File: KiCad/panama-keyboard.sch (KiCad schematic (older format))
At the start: 168 parts, among them J1 AVR-ISP-6, J2 USB_C_Receptacle_USB2.0, U1 ATmega32A-PU, Y1 Crystal

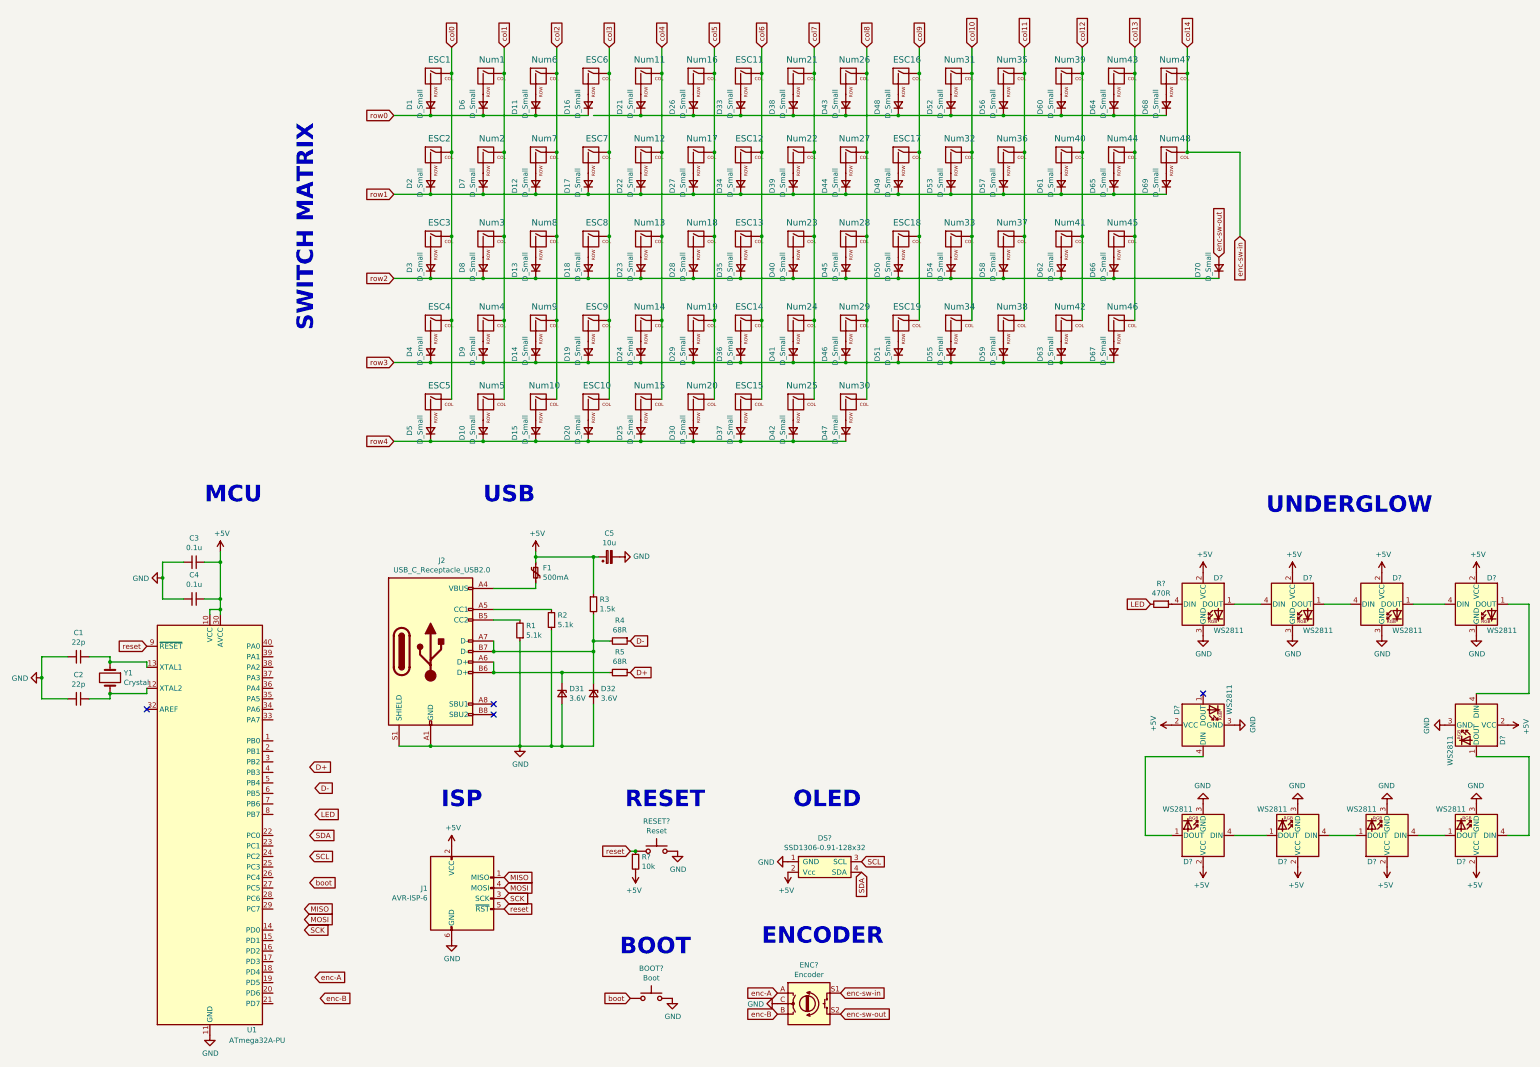
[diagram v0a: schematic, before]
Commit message: footprint added except MX
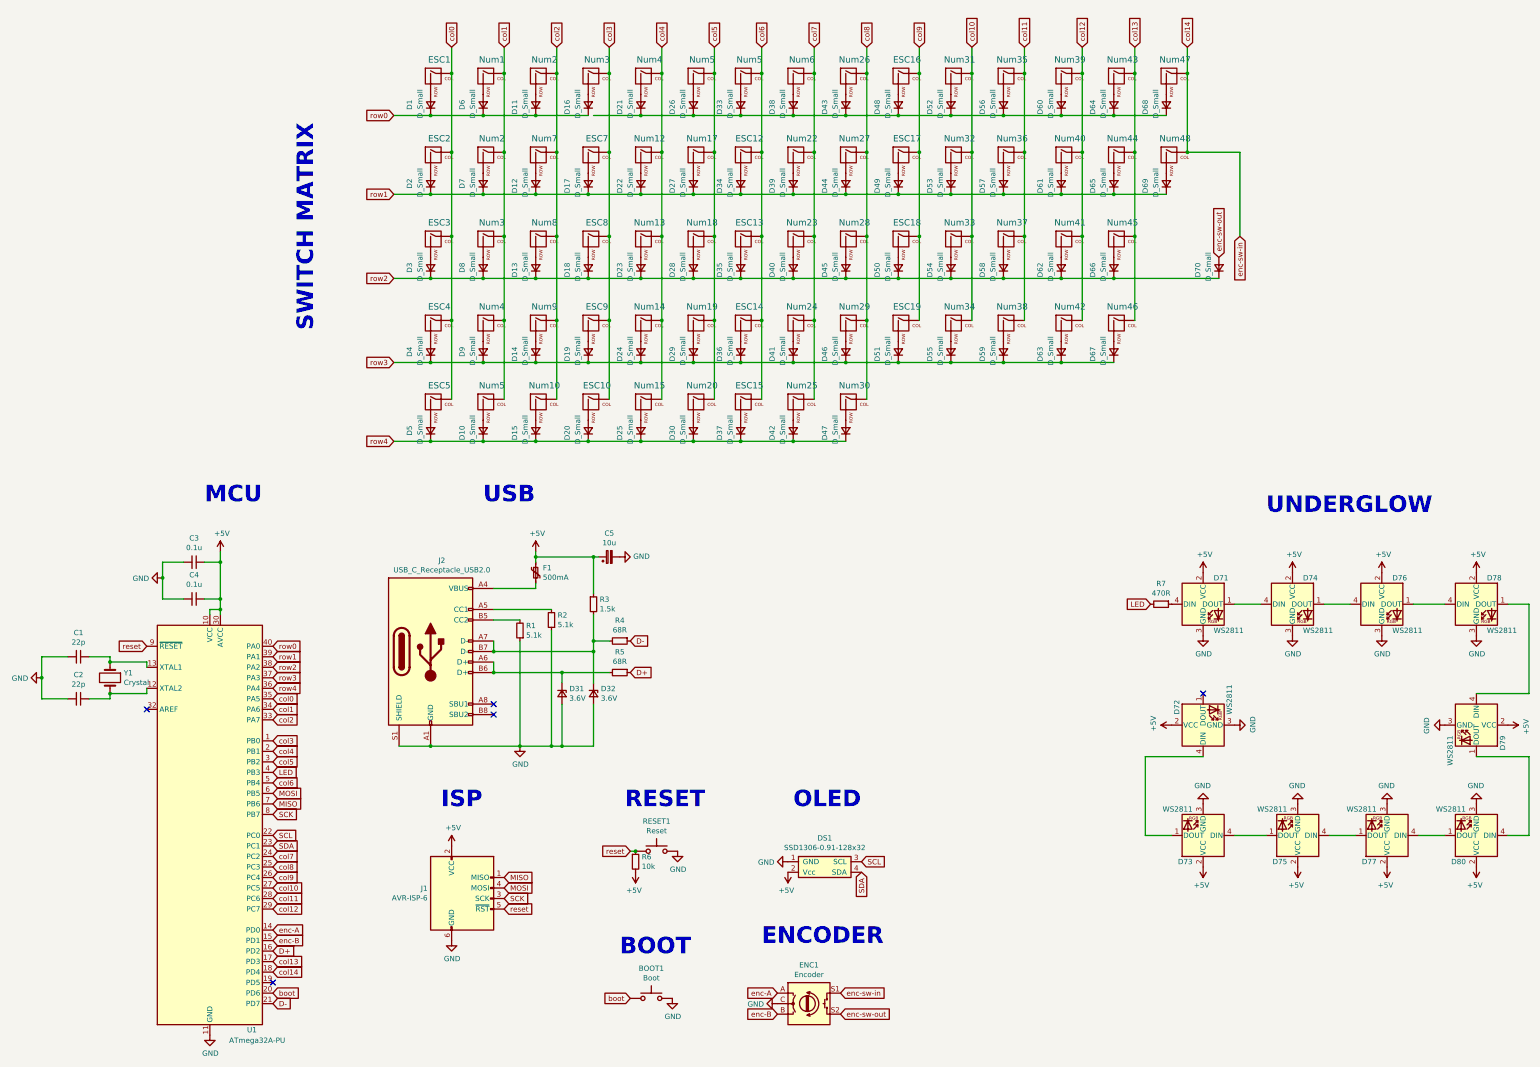
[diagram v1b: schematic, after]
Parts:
- BOOT1: renamed from BOOT?; footprint (none) -> Button_Switch_THT:SW_PUSH_6mm
- C1, C2, C3, C4: footprint (none) -> Capacitor_THT:C_Disc_D5.0mm_W2.5mm_P5.00mm
- C5: footprint (none) -> Capacitor_THT:CP_Radial_D5.0mm_P2.00mm
- D1, D10, D11, D12, D13, D14, D15, D16, D17, D18, D19, D2, D20, D21, D22, D23, D24, D25, D26, D27, D28, D29, D3, D30, D31, D32, D33, D34, D35, D36, D37, D38, D39, D4, D40, D41, D42, D43, D44, D45, D46, D47, D48, D49, D5, D50, D51, D52, D53, D54, D55, D56, D57, D58, D59, D6, D60, D61, D62, D63, D64, D65, D66, D67, D68, D69, D7, D70, D8, D9: footprint (none) -> Diode_THT:D_DO-35_SOD27_P7.62mm_Horizontal
- D71, D72, D73, D74, D75, D76, D77, D78, D79, D80: renamed from D?; footprint (none) -> LED_THT:LED_D5.0mm-4_RGB
- DS1: renamed from DS?; footprint (none) -> OLED:PinHeader_1x04_P2.54mm_Vertical
- ENC1: renamed from ENC?; footprint (none) -> Rotary_Encoder:RotaryEncoder_Alps_EC11E-Switch_Vertical_H20mm
- F1: footprint (none) -> Fuse:Fuse_BelFuse_0ZRE0005FF_L8.3mm_W3.8mm
- J1: footprint (none) -> Connector_PinHeader_2.54mm:PinHeader_2x03_P2.54mm_Vertical
- J2: footprint (none) -> Connector_USB:USB_C_Receptacle_GCT_USB4085
- R1, R2, R3, R4, R5: footprint (none) -> Resistor_THT:R_Axial_DIN0204_L3.6mm_D1.6mm_P5.08mm_Horizontal
- R6, R7: renamed from R?; footprint (none) -> Resistor_THT:R_Axial_DIN0204_L3.6mm_D1.6mm_P5.08mm_Horizontal
- RESET1: renamed from RESET?; footprint (none) -> Button_Switch_THT:SW_PUSH_6mm
- Y1: footprint (none) -> Crystal:Crystal_HC49-U_Vertical
- renumbered Num6 to Num2, ESC6 to Num3, Num11 to Num4, Num16 to Num5, ESC11 to Num5, Num21 to Num6
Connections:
- net D+: now also U1.16 (PD2)
- net D-: now also U1.21 (PD7)
- net LED: now also U1.4 (PB3)
- net MISO: now also U1.7 (PB6)
- net MOSI: now also U1.6 (PB5)
- net SCK: now also U1.8 (PB7)
- net SCL: now also U1.22 (PC0)
- net SDA: now also U1.23 (PC1)
- net boot: now also U1.20 (PD6)
- net col0: now also U1.35 (PA5)
- net col1: now also U1.34 (PA6)
- net col10: now also U1.27 (PC5)
- net col11: now also U1.28 (PC6)
- net col12: now also U1.29 (PC7)
- net col13: now also U1.17 (PD3)
- net col14: now also U1.18 (PD4)
- net col2: now also U1.33 (PA7)
- net col3: now also U1.1 (PB0)
- net col4: now also U1.2 (PB1)
- net col5: now also U1.3 (PB2)
- net col6: now also U1.5 (PB4)
- net col7: now also U1.24 (PC2)
- net col8: now also U1.25 (PC3)
- net col9: now also U1.26 (PC4)
- net enc-A: now also U1.14 (PD0)
- net enc-B: now also U1.15 (PD1)
- net row0: now also U1.40 (PA0)
- net row1: now also U1.39 (PA1)
- net row2: now also U1.38 (PA2)
- net row3: now also U1.37 (PA3)
- net row4: now also U1.36 (PA4)
- no-connect marks 4 -> 5

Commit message: finished w1 schematic, started PCB
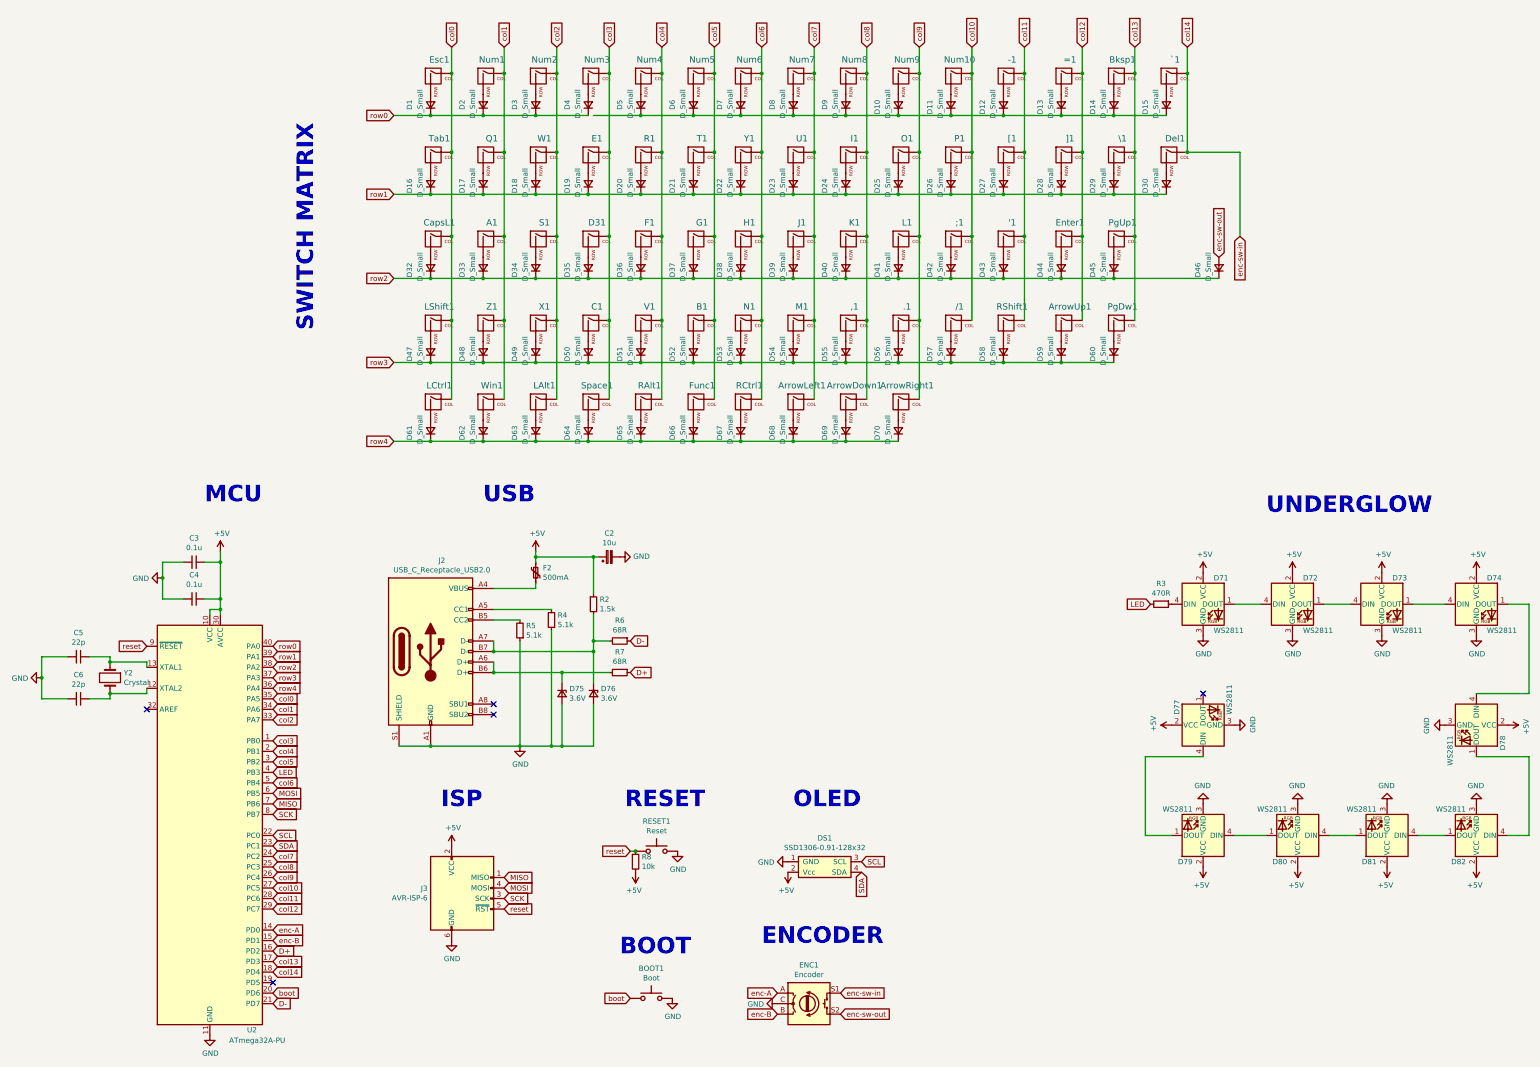
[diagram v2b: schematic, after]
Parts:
- added D67: D_Small, Diode_THT:D_DO-35_SOD27_P7.62mm_Horizontal, symbol Device:D_Small
- added RCtrl1: MX, Button_Switch_Keyboard:SW_Cherry_MX_1.00u_PCB, symbol Keyboard:MX
- '1: renamed from Num37; footprint (none) -> Button_Switch_Keyboard:SW_Cherry_MX_1.00u_PCB
- ,1: renamed from Num29; footprint (none) -> Button_Switch_Keyboard:SW_Cherry_MX_1.00u_PCB
- -1: renamed from Num35; footprint (none) -> Button_Switch_Keyboard:SW_Cherry_MX_1.00u_PCB
- .1: renamed from ESC19; footprint (none) -> Button_Switch_Keyboard:SW_Cherry_MX_1.00u_PCB
- /1: renamed from Num34; footprint (none) -> Button_Switch_Keyboard:SW_Cherry_MX_1.00u_PCB
- ;1: renamed from Num33; footprint (none) -> Button_Switch_Keyboard:SW_Cherry_MX_1.00u_PCB
- =1: renamed from Num39; footprint (none) -> Button_Switch_Keyboard:SW_Cherry_MX_1.00u_PCB
- A1: renamed from Num3; footprint (none) -> Button_Switch_Keyboard:SW_Cherry_MX_1.00u_PCB
- ArrowDown1: renamed from Num25; footprint (none) -> Button_Switch_Keyboard:SW_Cherry_MX_1.00u_PCB
- ArrowLeft1: renamed from ESC15; footprint (none) -> Button_Switch_Keyboard:SW_Cherry_MX_1.00u_PCB
- ArrowRight1: renamed from Num30; footprint (none) -> Button_Switch_Keyboard:SW_Cherry_MX_1.00u_PCB
- ArrowUp1: renamed from Num42; footprint (none) -> Button_Switch_Keyboard:SW_Cherry_MX_1.00u_PCB
- B1: renamed from Num19; footprint (none) -> Button_Switch_Keyboard:SW_Cherry_MX_1.00u_PCB
- Bksp1: renamed from Num43; footprint (none) -> Button_Switch_Keyboard:SW_Cherry_MX_2.00u_PCB
- C1: renamed from ESC9; footprint (none) -> Button_Switch_Keyboard:SW_Cherry_MX_1.00u_PCB
- CapsL1: renamed from ESC3; footprint (none) -> Button_Switch_Keyboard:SW_Cherry_MX_1.75u_PCB
- D31: renamed from ESC8; footprint (none) -> Button_Switch_Keyboard:SW_Cherry_MX_1.00u_PCB
- Del1: renamed from Num48; footprint (none) -> Button_Switch_Keyboard:SW_Cherry_MX_1.00u_PCB
- E1: renamed from ESC7; footprint (none) -> Button_Switch_Keyboard:SW_Cherry_MX_1.00u_PCB
- Enter1: renamed from Num41; footprint (none) -> Button_Switch_Keyboard:SW_Cherry_MX_2.25u_PCB
- Esc1: renamed from ESC1; footprint (none) -> Button_Switch_Keyboard:SW_Cherry_MX_1.00u_PCB
- F1: renamed from Num13; footprint (none) -> Button_Switch_Keyboard:SW_Cherry_MX_1.00u_PCB
- Func1: renamed from Num20; footprint (none) -> Button_Switch_Keyboard:SW_Cherry_MX_1.00u_PCB
- G1: renamed from Num18; footprint (none) -> Button_Switch_Keyboard:SW_Cherry_MX_1.00u_PCB
- H1: renamed from ESC13; footprint (none) -> Button_Switch_Keyboard:SW_Cherry_MX_1.00u_PCB
- I1: renamed from Num27; footprint (none) -> Button_Switch_Keyboard:SW_Cherry_MX_1.00u_PCB
- J1: renamed from Num23; footprint (none) -> Button_Switch_Keyboard:SW_Cherry_MX_1.00u_PCB
- K1: renamed from Num28; footprint (none) -> Button_Switch_Keyboard:SW_Cherry_MX_1.00u_PCB
- L1: renamed from ESC18; footprint (none) -> Button_Switch_Keyboard:SW_Cherry_MX_1.00u_PCB
- LAlt1: renamed from Num10; footprint (none) -> Button_Switch_Keyboard:SW_Cherry_MX_1.25u_PCB
- LCtrl1: renamed from ESC5; footprint (none) -> Button_Switch_Keyboard:SW_Cherry_MX_1.25u_PCB
- LShift1: renamed from ESC4; footprint (none) -> Button_Switch_Keyboard:SW_Cherry_MX_2.25u_PCB
- M1: renamed from Num24; footprint (none) -> Button_Switch_Keyboard:SW_Cherry_MX_1.00u_PCB
- N1: renamed from ESC14; footprint (none) -> Button_Switch_Keyboard:SW_Cherry_MX_1.00u_PCB
- Num1, Num2, Num3, Num4, Num5: footprint (none) -> Button_Switch_Keyboard:SW_Cherry_MX_1.00u_PCB
- Num10: renamed from Num31; footprint (none) -> Button_Switch_Keyboard:SW_Cherry_MX_1.00u_PCB
- Num6: renamed from Num5; footprint (none) -> Button_Switch_Keyboard:SW_Cherry_MX_1.00u_PCB
- Num7: renamed from Num6; footprint (none) -> Button_Switch_Keyboard:SW_Cherry_MX_1.00u_PCB
- Num8: renamed from Num26; footprint (none) -> Button_Switch_Keyboard:SW_Cherry_MX_1.00u_PCB
- Num9: renamed from ESC16; footprint (none) -> Button_Switch_Keyboard:SW_Cherry_MX_1.00u_PCB
- O1: renamed from ESC17; footprint (none) -> Button_Switch_Keyboard:SW_Cherry_MX_1.00u_PCB
- P1: renamed from Num32; footprint (none) -> Button_Switch_Keyboard:SW_Cherry_MX_1.00u_PCB
- PgDw1: renamed from Num46; footprint (none) -> Button_Switch_Keyboard:SW_Cherry_MX_1.00u_PCB
- PgUp1: renamed from Num45; footprint (none) -> Button_Switch_Keyboard:SW_Cherry_MX_1.00u_PCB
- Q1: renamed from Num2; footprint (none) -> Button_Switch_Keyboard:SW_Cherry_MX_1.00u_PCB
- R1: renamed from Num12; footprint (none) -> Button_Switch_Keyboard:SW_Cherry_MX_1.00u_PCB
- RAlt1: renamed from Num15; footprint (none) -> Button_Switch_Keyboard:SW_Cherry_MX_1.00u_PCB
- RShift1: renamed from Num38; footprint (none) -> Button_Switch_Keyboard:SW_Cherry_MX_1.75u_PCB
- S1: renamed from Num8; footprint (none) -> Button_Switch_Keyboard:SW_Cherry_MX_1.00u_PCB
- Space1: renamed from ESC10; footprint (none) -> Button_Switch_Keyboard:SW_Cherry_MX_6.25u_PCB
- T1: renamed from Num17; footprint (none) -> Button_Switch_Keyboard:SW_Cherry_MX_1.00u_PCB
- Tab1: renamed from ESC2; footprint (none) -> Button_Switch_Keyboard:SW_Cherry_MX_1.50u_PCB
- U1: renamed from Num22; footprint (none) -> Button_Switch_Keyboard:SW_Cherry_MX_1.00u_PCB
- V1: renamed from Num14; footprint (none) -> Button_Switch_Keyboard:SW_Cherry_MX_1.00u_PCB
- W1: renamed from Num7; footprint (none) -> Button_Switch_Keyboard:SW_Cherry_MX_1.00u_PCB
- Win1: renamed from Num5; footprint (none) -> Button_Switch_Keyboard:SW_Cherry_MX_1.25u_PCB
- X1: renamed from Num9; footprint (none) -> Button_Switch_Keyboard:SW_Cherry_MX_1.00u_PCB
- Y1: renamed from ESC12; footprint (none) -> Button_Switch_Keyboard:SW_Cherry_MX_1.00u_PCB
- Z1: renamed from Num4; footprint (none) -> Button_Switch_Keyboard:SW_Cherry_MX_1.00u_PCB
- [1: renamed from Num36; footprint (none) -> Button_Switch_Keyboard:SW_Cherry_MX_1.00u_PCB
- \1: renamed from Num44; footprint (none) -> Button_Switch_Keyboard:SW_Cherry_MX_1.50u_PCB
- ]1: renamed from Num40; footprint (none) -> Button_Switch_Keyboard:SW_Cherry_MX_1.00u_PCB
- `1: renamed from Num47; footprint (none) -> Button_Switch_Keyboard:SW_Cherry_MX_1.00u_PCB
- renumbered C5 to C2, C1 to C5, C2 to C6, D48 to D10, D52 to D11, D56 to D12, D60 to D13, D64 to D14, D68 to D15, D2 to D16, D7 to D17, D12 to D18, D17 to D19, D6 to D2, D22 to D20, D27 to D21, D34 to D22, D39 to D23, D44 to D24, D49 to D25, D53 to D26, D57 to D27, D61 to D28, D65 to D29, D11 to D3, D69 to D30, D3 to D32, D8 to D33, D13 to D34, D18 to D35, D23 to D36, D28 to D37, D35 to D38, D40 to D39, D16 to D4, D45 to D40, D50 to D41, D54 to D42, D58 to D43, D62 to D44, D66 to D45, D70 to D46, D4 to D47, D9 to D48, D14 to D49, D21 to D5, D19 to D50, D24 to D51, D29 to D52, D36 to D53, D41 to D54, D46 to D55, D51 to D56, D55 to D57, D59 to D58, D63 to D59, D26 to D6, D67 to D60, D5 to D61, D10 to D62, D15 to D63, D20 to D64, D25 to D65, D30 to D66, D37 to D68, D42 to D69, D33 to D7, D47 to D70, D74 to D72, D76 to D73, D78 to D74, D31 to D75, D32 to D76, D72 to D77, D79 to D78, D73 to D79, D38 to D8, D75 to D80, D77 to D81, D80 to D82, D43 to D9, F1 to F2, J1 to J3, R3 to R2, R7 to R3, R2 to R4, R1 to R5, R4 to R6, R5 to R7, R6 to R8, U1 to U2, Y1 to Y2
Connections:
- net col6: now also RCtrl1.1 (COL); no longer ArrowLeft1.1 (COL)
- net col7: now also ArrowLeft1.1 (COL); no longer ArrowDown1.1 (COL)
- net col8: now also ArrowDown1.1 (COL); no longer ArrowRight1.1 (COL)
- net col9: now also ArrowRight1.1 (COL)
- net row4: now also D67.1 (K)
- new net: D67.2 (A), RCtrl1.2 (ROW)
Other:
- moved on the sheet: ArrowDown1, ArrowLeft1, ArrowRight1, D68, D69, D70

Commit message: progree pcb
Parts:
- DS1: footprint OLED:PinHeader_1x04_P2.54mm_Vertical -> OLED:OLED_0.91in_128x32
- U2: footprint Package_DIP:DIP-40_W15.24mm -> Package_DIP:DIP-40_W15.24mm_Socket
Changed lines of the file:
@@
 F 0 "U2" H 3100 6650 50  0000 C CNN
 F 1 "ATmega32A-PU" H 3150 6550 50  0000 C CNN
-F 2 "Package_DIP:DIP-40_W15.24mm" H 2700 8600 50  0001 C CIN
+F 2 "Package_DIP:DIP-40_W15.24mm_Socket" H 2700 8600 50  0001 C CIN
 F 3 "http://ww1.microchip.com/downloads/en/DeviceDoc/atmel-8155-8-bit-microcontroller-avr-atmega32a_datasheet.pdf" H 2700 8600 50  0001 C CNN
 	1    2700 8600
@@
 F 0 "DS1" H 8550 9275 50  0000 C CNN
 F 1 "SSD1306-0.91-128x32" H 8550 9184 50  0000 C CNN
-F 2 "OLED:PinHeader_1x04_P2.54mm_Vertical" H 8550 9000 50  0001 C CNN
+F 2 "OLED:OLED_0.91in_128x32" H 8550 9000 50  0001 C CNN
 F 3 "" H 8550 9000 50  0001 C CNN
 	1    8550 9000

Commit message: pcb progress, back to 10 leds
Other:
- moved on the sheet: D71, D72, D73, D74, D77, D78, D79, D80, D81, D82, R3
